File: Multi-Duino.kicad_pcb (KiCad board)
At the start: 4 copper layers, 68.6 x 53.3 mm, 67 parts, among them J1 M20-9980345, J10 Micro_SD_Card_Det1, J2 M20-9980245, J3 M20-9980345, J4 PPTC101LFBN-RC, J5 PPTC081LFBN-RC, J6 PPTC061LFBN-RC, J7 PPTC081LFBN-RC, J8 USB_C_Receptacle_USB2.0_16P, Q1 FDN340P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

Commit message: Update Multiduino v2 design
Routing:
- net +5V: track 0.00 -> 13.7 mm
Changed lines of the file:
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@@
 		)
+	)
+	(segment
+		(start 152.3111 124.3033)
+		(end 151.8582 123.8504)
+		(width 0.7)
+		(layer "F.Cu")
+		(net 2)
+	)
+	(segment
+		(start 152.3111 126)
+		(end 152.3111 124.3033)
+		(width 0.7)
+		(layer "F.Cu")
+		(net 2)
+	)
+	(segment
+		(start 155 126)
+		(end 152.3111 126)
+		(width 0.7)
+		(layer "F.Cu")
+		(net 2)
+	)
+	(segment
+		(start 152.3111 129.1336)
+		(end 152.3111 126)
+		(width 0.7)
+		(layer "F.Cu")
+		(net 2)
+	)
+	(segment
+		(start 156.9717 121.2596)
+		(end 156.9717 124.0283)
+		(width 0.7)
+		(layer "F.Cu")
+		(net 2)
+	)
+	(segment
+		(start 156.9717 124.0283)
+		(end 155 126)
+		(width 0.7)
+		(layer "F.Cu")
+		(net 2)
 	)
 	(zone

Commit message: Update Multiduino v2 design
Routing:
- net +5V: track 13.7 -> 37.2 mm
- net +3.3V: track 0.00 -> 14.7 mm
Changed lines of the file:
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@@
+	)
+	(segment
+		(start 132.01525 110.752)
+		(end 133.61325 109.154)
+		(width 0.7)
+		(layer "F.Cu")
+		(net 2)
 	)
 	(segment
@@
 	)
 	(segment
+		(start 130.45 115.8)
+		(end 131.988 114.262)
+		(width 0.7)
+		(layer "F.Cu")
+		(net 2)
+	)
+	(segment
+		(start 131.988 110.752)
+		(end 132.01525 110.752)
+		(width 0.7)
+		(layer "F.Cu")
+		(net 2)
+	)
+	(segment
+		(start 135.75 115.8)
+		(end 138.4 115.8)
+		(width 0.7)
+		(layer "F.Cu")
+		(net 2)
+	)
+	(segment
 		(start 155 126)
 		(end 152.3111 126)
+		(width 0.7)
+		(layer "F.Cu")
+		(net 2)
+	)
+	(segment
+		(start 133.61325 109.154)
+		(end 134.4065 109.154)
+		(width 0.7)
+		(layer "F.Cu")
+		(net 2)
+	)
+	(segment
+		(start 131.988 114.262)
+		(end 131.988 110.752)
 		(width 0.7)
 		(layer "F.Cu")
@@
 	)
 	(segment
+		(start 135.75 112.3975)
+		(end 134.4065 111.054)
+		(width 0.7)
+		(layer "F.Cu")
+		(net 2)
+	)
+	(segment
 		(start 156.9717 121.2596)
 		(end 156.9717 124.0283)
+		(width 0.7)
+		(layer "F.Cu")
+		(net 2)
+	)
+	(segment
+		(start 138.4 115.8)
+		(end 140.7 113.5)
+		(width 0.7)
+		(layer "F.Cu")
+		(net 2)
+	)
+	(segment
+		(start 129.45 115.8)
+		(end 130.45 115.8)
+		(width 0.7)
+		(layer "F.Cu")
+		(net 2)
+	)
+	(segment
+		(start 131.988 110.752)
+		(end 132.29 111.054)
+		(width 0.7)
+		(layer "F.Cu")
+		(net 2)
+	)
+	(segment
+		(start 135.75 115.8)
+		(end 135.75 112.3975)
+		(width 0.7)
+		(layer "F.Cu")
+		(net 2)
+	)
+	(segment
+		(start 132.29 111.054)
+		(end 134.4065 111.054)
 		(width 0.7)
 		(layer "F.Cu")
@@
 		(net 2)
 	)
+	(segment
+		(start 135.8295 108.302)
+		(end 136.6815 109.154)
+		(width 0.5)
+		(layer "F.Cu")
+		(net 4)
+	)
+	(segment
+		(start 126.568088 106.35)
+		(end 128.520088 108.302)
+		(width 0.5)
+		(layer "F.Cu")
+		(net 4)
+	)
+	(segment
+		(start 139.1 109.202)
+		(end 136.7295 109.202)
+		(width 0.7)
+		(layer "F.Cu")
+		(net 4)
+	)
+	(segment
+		(start 128.520088 108.302)
+		(end 135.8295 108.302)
+		(width 0.5)
+		(layer "F.Cu")
+		(net 4)
+	)
+	(segment
+		(start 136.7295 109.202)
+		(end 136.6815 109.154)
+		(width 0.7)
+		(layer "F.Cu")
+		(net 4)
+	)
+	(segment
+		(start 125.625 106.35)
+		(end 126.568088 106.35)
+		(width 0.5)
+		(layer "F.Cu")
+		(net 4)
+	)
 	(zone

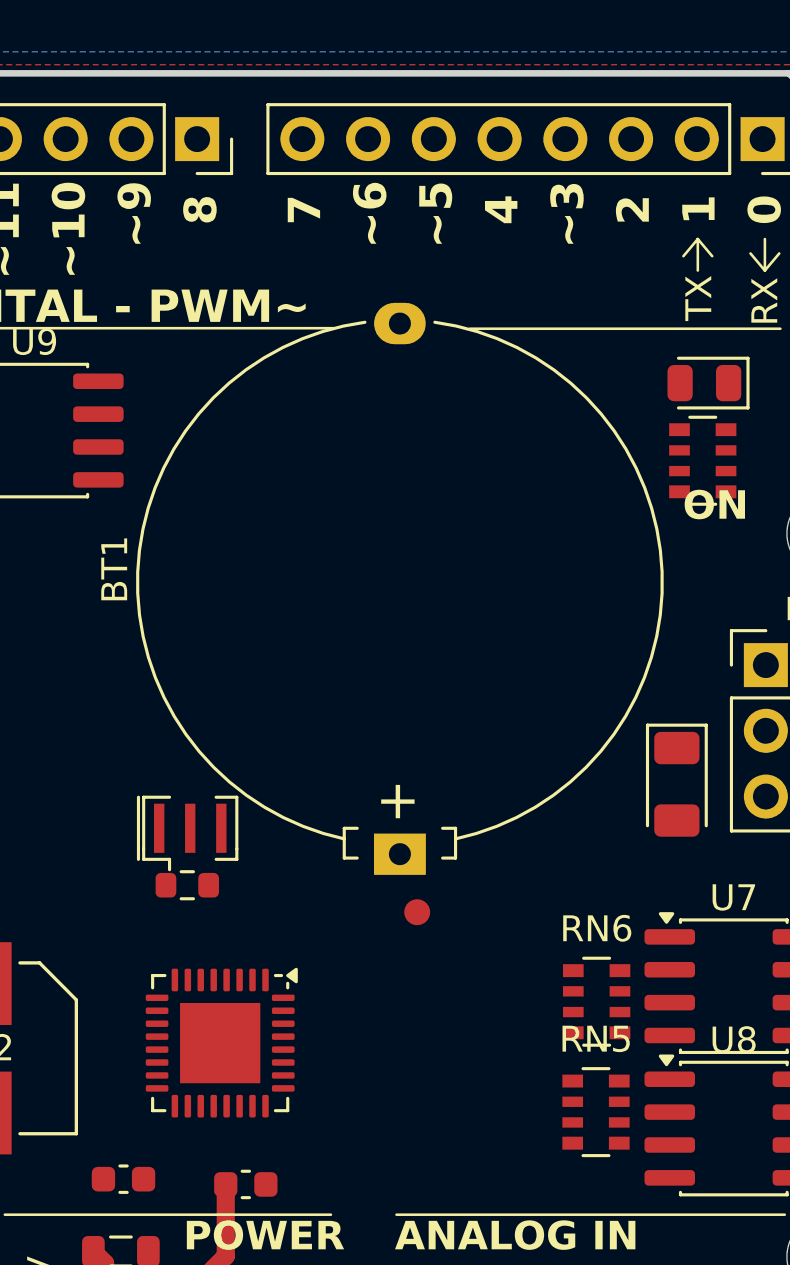
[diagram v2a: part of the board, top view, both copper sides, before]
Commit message: Update Multiduino v2 design
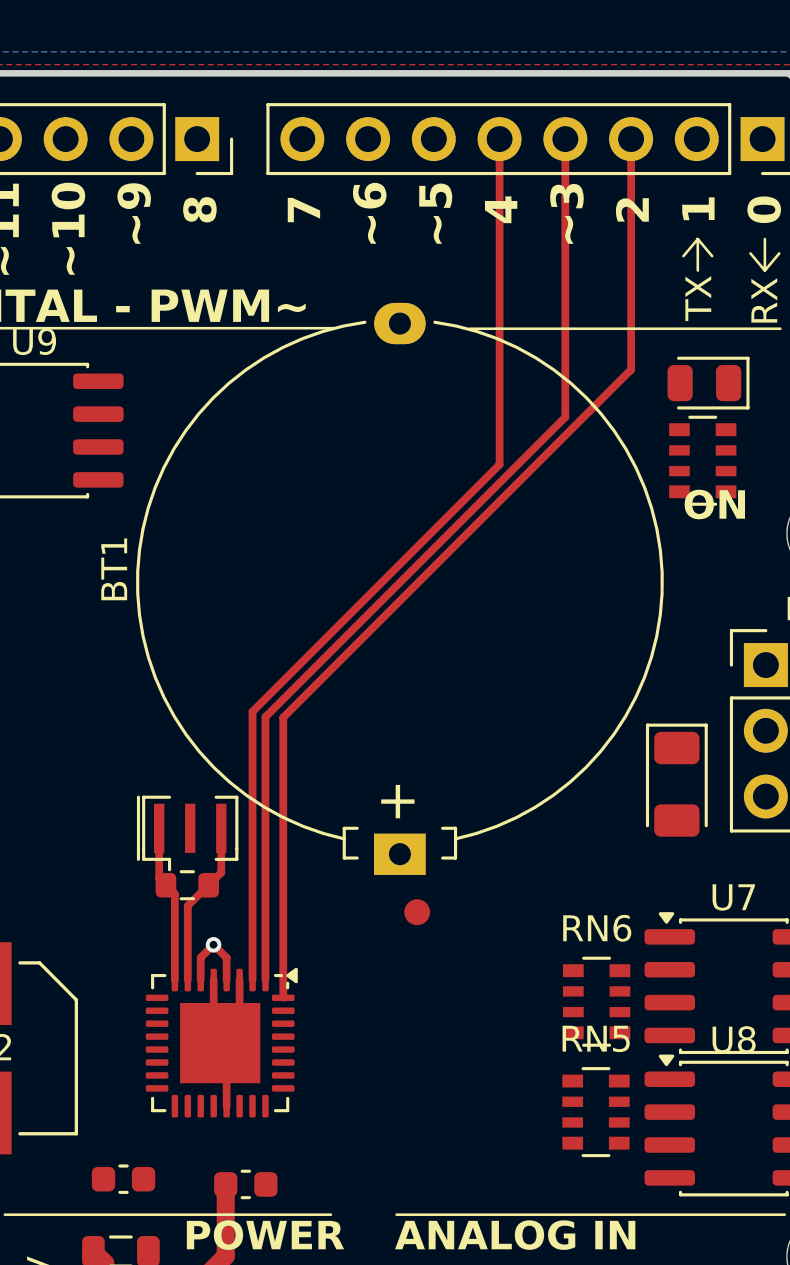
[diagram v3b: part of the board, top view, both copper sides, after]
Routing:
- net IO2: track 0.00 -> 38.7 mm
- net IO3: track 0.00 -> 37.3 mm
- net IO4: track 0.00 -> 36.4 mm
- net GND: track 0.00 -> 7.83 mm
- net Net-(U4-PB6): track 0.00 -> 6.40 mm
- net Net-(U4-PB7): track 0.00 -> 6.11 mm
- net +5V: track 37.2 -> 40.4 mm, vias 0 -> 1
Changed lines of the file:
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@@
+	)
+	(segment
+		(start 157.5061 115.0486)
+		(end 156.7561 115.7986)
+		(width 0.3)
+		(layer "F.Cu")
+		(net 1)
+	)
+	(segment
+		(start 157.0061 118.2361)
+		(end 157.0061 116.0486)
+		(width 0.3)
+		(layer "F.Cu")
+		(net 1)
+	)
+	(segment
+		(start 157.0061 116.0486)
+		(end 156.7561 115.7986)
+		(width 0.3)
+		(layer "F.Cu")
+		(net 1)
+	)
+	(segment
+		(start 157.5061 113.3611)
+		(end 157.5061 115.0486)
+		(width 0.3)
+		(layer "F.Cu")
+		(net 1)
+	)
+	(segment
+		(start 156.5061 115.5486)
+		(end 156.7561 115.7986)
+		(width 0.3)
+		(layer "F.Cu")
+		(net 1)
+	)
+	(segment
+		(start 156.5061 113.3611)
+		(end 156.5061 115.5486)
+		(width 0.3)
+		(layer "F.Cu")
+		(net 1)
 	)
 	(segment
@@
 	)
 	(segment
+		(start 157.0061 112.5061)
+		(end 157.0061 113.3611)
+		(width 0.3)
+		(layer "F.Cu")
+		(net 2)
+	)
+	(segment
 		(start 152.3111 126)
 		(end 152.3111 124.3033)
@@
 	)
 	(segment
+		(start 156.5 112)
+		(end 157.0061 112.5061)
+		(width 0.3)
+		(layer "F.Cu")
+		(net 2)
+	)
+	(segment
 		(start 130.45 115.8)
 		(end 131.988 114.262)
@@
 	)
 	(segment
+		(start 156.0061 113.3611)
+		(end 156.0061 112.4939)
+		(width 0.3)
+		(layer "F.Cu")
+		(net 2)
+	)
+	(segment
 		(start 133.61325 109.154)
 		(end 134.4065 109.154)
@@
 	)
 	(segment
+		(start 156.0061 112.4939)
+		(end 156.5 112)
+		(width 0.3)
+		(layer "F.Cu")
+		(net 2)
+	)
+	(segment
 		(start 135.75 112.3975)
 		(end 134.4065 111.054)
@@
 		(width 0.7)
 		(layer "F.Cu")
+		(net 2)
+	)
+	(via
+		(at 156.5 112)
+		(size 0.6)
+		(drill 0.3)
+		(layers "F.Cu" "B.Cu")
 		(net 2)
 	)
@@
 		(net 4)
 	)
+	(segment
+		(start 158.0061 113.3611)
+		(end 158.0061 102.9939)
+		(width 0.3)
+		(layer "F.Cu")
+		(net 40)
+	)
+	(segment
+		(start 167.5511 93.4489)
+		(end 167.5511 80.8736)
+		(width 0.3)
+		(layer "F.Cu")
+		(net 40)
+	)
+	(segment
+		(start 158.0061 102.9939)
+		(end 167.5511 93.4489)
+		(width 0.3)
+		(layer "F.Cu")
+		(net 40)
+	)
+	(segment
+		(start 158.5061 103.201006)
+		(end 170.0911 91.616006)
+		(width 0.3)
+		(layer "F.Cu")
+		(net 41)
+	)
+	(segment
+		(start 170.0911 91.616006)
+		(end 170.0911 80.8736)
+		(width 0.3)
+		(layer "F.Cu")
+		(net 41)
+	)
+	(segment
+		(start 158.5061 113.3611)
+		(end 158.5061 103.201006)
+		(width 0.3)
+		(layer "F.Cu")
+		(net 41)
+	)
+	(segment
+		(start 172.6311 89.783112)
+		(end 172.6311 80.8736)
+		(width 0.3)
+		(layer "F.Cu")
+		(net 42)
+	)
+	(segment
+		(start 159.1936 114.0486)
+		(end 159.1936 103.220612)
+		(width 0.3)
+		(layer "F.Cu")
+		(net 42)
+	)
+	(segment
+		(start 159.1936 103.220612)
+		(end 172.6311 89.783112)
+		(width 0.3)
+		(layer "F.Cu")
+		(net 42)
+	)
+	(segment
+		(start 155.0061 113.3611)
+		(end 155.0061 110.045)
+		(width 0.3)
+		(layer "F.Cu")
+		(net 58)
+	)
+	(segment
+		(start 155.0061 110.045)
+		(end 154.6611 109.7)
+		(width 0.3)
+		(layer "F.Cu")
+		(net 58)
+	)
+	(segment
+		(start 154.4 107.5)
+		(end 154.4 109.4389)
+		(width 0.3)
+		(layer "F.Cu")
+		(net 58)
+	)
+	(segment
+		(start 154.4 109.4389)
+		(end 154.6611 109.7)
+		(width 0.3)
+		(layer "F.Cu")
+		(net 58)
+	)
+	(segment
+		(start 156.8 107.5)
+		(end 156.8 109.2111)
+		(width 0.3)
+		(layer "F.Cu")
+		(net 59)
+	)
+	(segment
+		(start 156.3 109.7)
+		(end 156.3111 109.7)
+		(width 0.3)
+		(layer "F.Cu")
+		(net 59)
+	)
+	(segment
+		(start 155.5061 110.4939)
+		(end 156.3 109.7)
+		(width 0.3)
+		(layer "F.Cu")
+		(net 59)
+	)
+	(segment
+		(start 155.5061 113.3611)
+		(end 155.5061 110.4939)
+		(width 0.3)
+		(layer "F.Cu")
+		(net 59)
+	)
+	(segment
+		(start 156.8 109.2111)
+		(end 156.3111 109.7)
+		(width 0.3)
+		(layer "F.Cu")
+		(net 59)
+	)
 	(zone

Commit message: Update Multiduino v2 design
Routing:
- added copper zone on In1.Cu, net A4/SDA
- added copper zone on In2.Cu, net A5/SCL
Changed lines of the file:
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@@
+		)
+	)
+	(zone
+		(net 34)
+		(net_name "A4{slash}SDA")
+		(layer "In1.Cu")
+		(hatch none 0.5)
+		(connect_pads yes
+			(clearance 0.3)
+		)
+		(min_thickness 0.25)
+		(filled_areas_thickness no)
+		(fill yes
+			(thermal_gap 0.5)
+			(thermal_bridge_width 0.5)
+		)
+		(polygon
+			(pts
+				(xy 112.5 76.5) (xy 185.5 76.5) (xy 185.5 133.5) (xy 112.5 133.5)
+			)
+		)
+	)
+	(zone
+		(net 36)
+		(net_name "A5{slash}SCL")
+		(layer "In2.Cu")
+		(hatch none 0.5)
+		(connect_pads yes
+			(clearance 0.3)
+		)
+		(min_thickness 0.25)
+		(filled_areas_thickness no)
+		(fill yes
+			(thermal_gap 0.5)
+			(thermal_bridge_width 0.5)
+		)
+		(polygon
+			(pts
+				(xy 112 76) (xy 186 76) (xy 186 134) (xy 112 134)
+			)
 		)
 	)

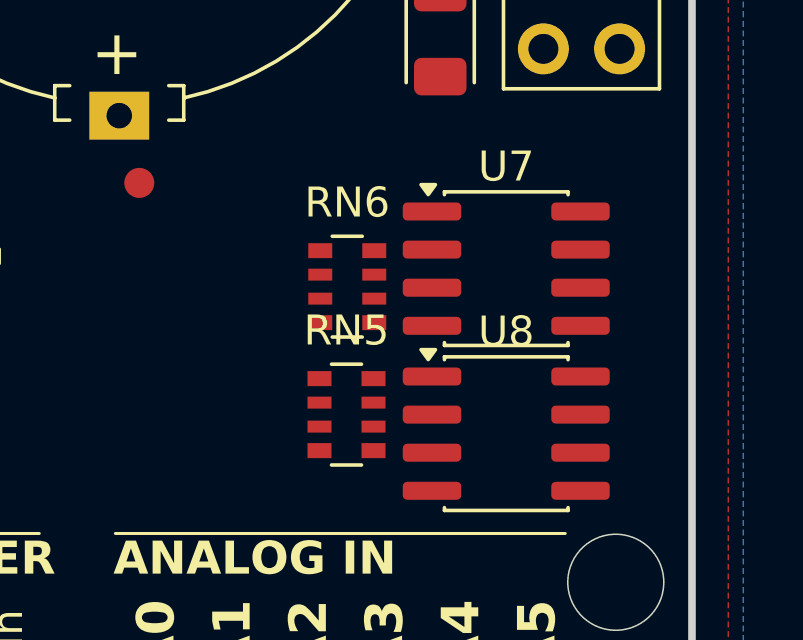
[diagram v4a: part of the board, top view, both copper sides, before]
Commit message: Update Multiduino v2 design
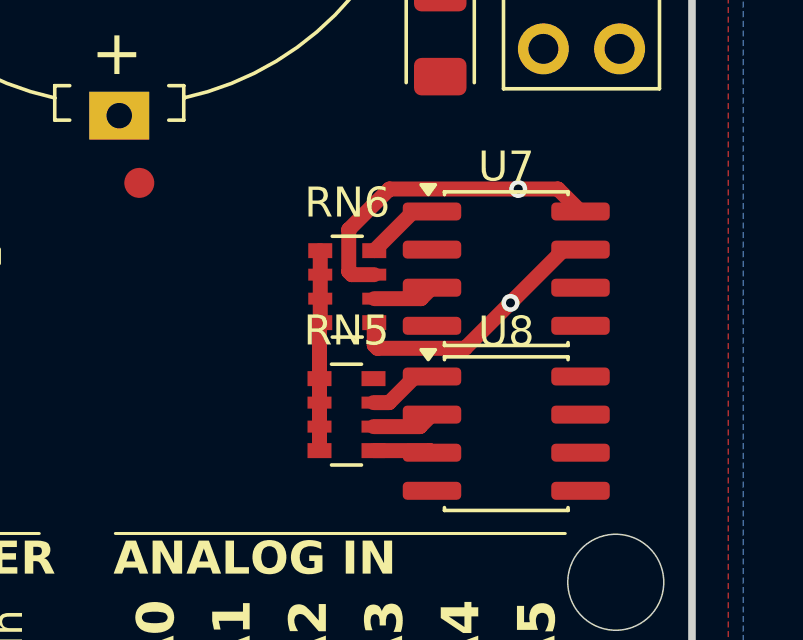
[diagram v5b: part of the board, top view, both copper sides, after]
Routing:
- net A5/SCL: track 0.00 -> 10.9 mm, vias 0 -> 1
- net A4/SDA: track 0.00 -> 9.03 mm, vias 0 -> 1
- net +5V: track 40.4 -> 47.0 mm
- net 32K: track 0.00 -> 2.47 mm
- net Net-(JP3-B): track 0.00 -> 2.31 mm
- net Net-(JP4-B): track 0.00 -> 2.12 mm
- net SQW: track 0.00 -> 2.08 mm
- net Net-(JP5-B): track 0.00 -> 1.98 mm
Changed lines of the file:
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@@
+	)
+	(segment
+		(start 170.375 118.865)
+		(end 170.375 118.065)
+		(width 0.5)
+		(layer "F.Cu")
+		(net 2)
+	)
+	(segment
+		(start 170.375 117.265)
+		(end 170.375 115.425)
+		(width 0.5)
+		(layer "F.Cu")
+		(net 2)
+	)
+	(segment
+		(start 170.375 118.065)
+		(end 170.375 117.265)
+		(width 0.5)
+		(layer "F.Cu")
+		(net 2)
 	)
 	(segment
@@
 	)
 	(segment
+		(start 170.4 115.4)
+		(end 170.4 114.6)
+		(width 0.5)
+		(layer "F.Cu")
+		(net 2)
+	)
+	(segment
 		(start 131.988 110.752)
 		(end 132.01525 110.752)
@@
 	)
 	(segment
+		(start 170.375 119.665)
+		(end 170.375 118.865)
+		(width 0.5)
+		(layer "F.Cu")
+		(net 2)
+	)
+	(segment
 		(start 156.0061 113.3611)
 		(end 156.0061 112.4939)
@@
 	)
 	(segment
+		(start 170.375 115.425)
+		(end 170.4 115.4)
+		(width 0.5)
+		(layer "F.Cu")
+		(net 2)
+	)
+	(segment
 		(start 129.45 115.8)
 		(end 130.45 115.8)
@@
 	)
 	(segment
+		(start 170.4 114.6)
+		(end 170.4 113.8)
+		(width 0.5)
+		(layer "F.Cu")
+		(net 2)
+	)
+	(segment
 		(start 132.29 111.054)
 		(end 134.4065 111.054)
 		(width 0.7)
+		(layer "F.Cu")
+		(net 2)
+	)
+	(segment
+		(start 170.4 113.8)
+		(end 170.4 113)
+		(width 0.5)
 		(layer "F.Cu")
 		(net 2)
@@
 	)
 	(segment
+		(start 176.741158 114.741158)
+		(end 178.517316 112.965)
+		(width 0.5)
+		(layer "F.Cu")
+		(net 34)
+	)
+	(segment
+		(start 172.2 116.15)
+		(end 172.305 116.255)
+		(width 0.5)
+		(layer "F.Cu")
+		(net 34)
+	)
+	(segment
+		(start 175.227316 116.255)
+		(end 176.741158 114.741158)
+		(width 0.5)
+		(layer "F.Cu")
+		(net 34)
+	)
+	(segment
+		(start 172.305 116.255)
+		(end 175.227316 116.255)
+		(width 0.5)
+		(layer "F.Cu")
+		(net 34)
+	)
+	(segment
+		(start 172.2 115.4)
+		(end 172.2 116.15)
+		(width 0.5)
+		(layer "F.Cu")
+		(net 34)
+	)
+	(segment
+		(start 178.517316 112.965)
+		(end 179.075 112.965)
+		(width 0.5)
+		(layer "F.Cu")
+		(net 34)
+	)
+	(via
+		(at 176.741158 114.741158)
+		(size 0.6)
+		(drill 0.3)
+		(layers "F.Cu" "B.Cu")
+		(net 34)
+	)
+	(segment
+		(start 178.325 110.945)
+		(end 179.075 111.695)
+		(width 0.5)
+		(layer "F.Cu")
+		(net 36)
+	)
+	(segment
+		(start 171.35 113.7)
+		(end 171.35 112.3)
+		(width 0.5)
+		(layer "F.Cu")
+		(net 36)
+	)
+	(segment
+		(start 172.705 110.945)
+		(end 177 110.945)
+		(width 0.5)
+		(layer "F.Cu")
+		(net 36)
+	)
+	(segment
+		(start 177 110.945)
+		(end 178.325 110.945)
+		(width 0.5)
+		(layer "F.Cu")
+		(net 36)
+	)
+	(segment
+		(start 172.2 113.8)
+		(end 171.45 113.8)
+		(width 0.5)
+		(layer "F.Cu")
+		(net 36)
+	)
+	(segment
+		(start 171.35 112.3)
+		(end 172.705 110.945)
+		(width 0.5)
+		(layer "F.Cu")
+		(net 36)
+	)
+	(segment
+		(start 171.45 113.8)
+		(end 171.35 113.7)
+		(width 0.5)
+		(layer "F.Cu")
+		(net 36)
+	)
+	(via
+		(at 177 110.945)
+		(size 0.6)
+		(drill 0.3)
+		(layers "F.Cu" "B.Cu")
+		(net 36)
+	)
+	(segment
 		(start 158.0061 113.3611)
 		(end 158.0061 102.9939)
@@
 		(net 59)
 	)
+	(segment
+		(start 172.2 114.6)
+		(end 173.76 114.6)
+		(width 0.5)
+		(layer "F.Cu")
+		(net 93)
+	)
+	(segment
+		(start 173.76 114.6)
+		(end 174.125 114.235)
+		(width 0.5)
+		(layer "F.Cu")
+		(net 93)
+	)
+	(segment
+		(start 172.2 113)
+		(end 173.505 111.695)
+		(width 0.5)
+		(layer "F.Cu")
+		(net 95)
+	)
+	(segment
+		(start 173.505 111.695)
+		(end 174.125 111.695)
+		(width 0.5)
+		(layer "F.Cu")
+		(net 95)
+	)
+	(segment
+		(start 172.175 118.865)
+		(end 173.725 118.865)
+		(width 0.5)
+		(layer "F.Cu")
+		(net 96)
+	)
+	(segment
+		(start 173.725 118.865)
+		(end 174.125 118.465)
+		(width 0.5)
+		(layer "F.Cu")
+		(net 96)
+	)
+	(segment
+		(start 172.175 119.665)
+		(end 174.055 119.665)
+		(width 0.5)
+		(layer "F.Cu")
+		(net 97)
+	)
+	(segment
+		(start 174.055 119.665)
+		(end 174.125 119.735)
+		(width 0.5)
+		(layer "F.Cu")
+		(net 97)
+	)
+	(segment
+		(start 172.175 118.065)
+		(end 172.697316 118.065)
+		(width 0.5)
+		(layer "F.Cu")
+		(net 98)
+	)
+	(segment
+		(start 173.567316 117.195)
+		(end 174.125 117.195)
+		(width 0.5)
+		(layer "F.Cu")
+		(net 98)
+	)
+	(segment
+		(start 172.697316 118.065)
+		(end 173.567316 117.195)
+		(width 0.5)
+		(layer "F.Cu")
+		(net 98)
+	)
 	(zone
